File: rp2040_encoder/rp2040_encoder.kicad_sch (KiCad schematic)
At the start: 14 parts, among them J1 Conn_01x05, U1 MT6701, U2 love

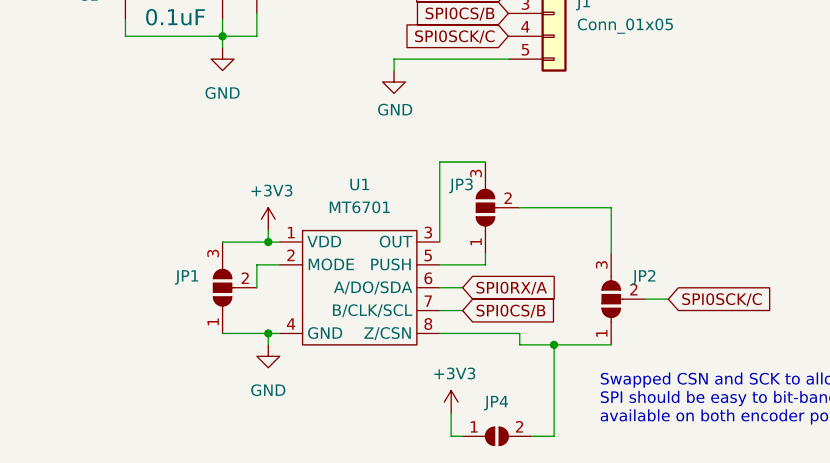
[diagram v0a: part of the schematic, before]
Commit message: updated design with dual CPUs
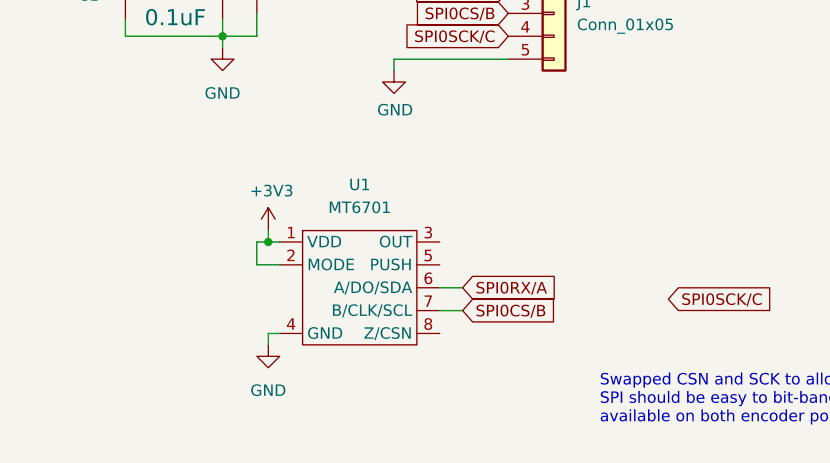
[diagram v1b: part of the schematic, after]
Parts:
- removed JP1, JP2, JP3: SolderJumper_3_Open, Jumper:SolderJumper-3_P1.3mm_Open_RoundedPad1.0x1.5mm_NumberLabels, symbol Jumper:SolderJumper_3_Open
- removed JP4: SolderJumper_2_Open, Jumper:SolderJumper-2_P1.3mm_Open_RoundedPad1.0x1.5mm, symbol Jumper:SolderJumper_2_Open
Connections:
- net +3V3: now also U1.2 (MODE)
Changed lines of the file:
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@@
 (kicad_sch (version 20211123) (generator eeschema)
   (paper "A4")
-  (junction (at 153.67 121.92) (diameter 0) (color 0 0 0 0)
-  )
-  (junction (at 121.92 120.65) (diameter 0) (color 0 0 0 0)
+  (junction (at 121.92 110.49) (diameter 0) (color 0 0 0 0)
   )
   (junction (at 116.84 76.2) (diameter 0) (color 0 0 0 0)
   )
-  (junction (at 121.92 110.49) (diameter 0) (color 0 0 0 0)
-  )
   (junction (at 116.84 87.63) (diameter 0) (color 0 0 0 0)
   )
@@
     (stroke (width 0) (type default) (color 0 0 0 0))
   )
-  (wire (pts (xy 140.97 110.49) (xy 140.97 101.6))
-    (stroke (width 0) (type default) (color 0 0 0 0))
-  )
   (wire (pts (xy 123.19 110.49) (xy 121.92 110.49))
     (stroke (width 0) (type default) (color 0 0 0 0))
   )
-  (wire (pts (xy 160.02 106.68) (xy 160.02 111.76))
-    (stroke (width 0) (type default) (color 0 0 0 0))
-  )
   (wire (pts (xy 120.65 87.63) (xy 120.65 85.09))
     (stroke (width 0) (type default) (color 0 0 0 0))
@@
     (stroke (width 0) (type default) (color 0 0 0 0))
   )
-  (wire (pts (xy 149.86 106.68) (xy 160.02 106.68))
-    (stroke (width 0) (type default) (color 0 0 0 0))
-  )
-  (wire (pts (xy 120.65 113.03) (xy 120.65 115.57))
-    (stroke (width 0) (type default) (color 0 0 0 0))
-  )
   (wire (pts (xy 116.84 76.2) (xy 116.84 78.105))
     (stroke (width 0) (type default) (color 0 0 0 0))
   )
-  (wire (pts (xy 140.97 113.03) (xy 146.05 113.03))
-    (stroke (width 0) (type default) (color 0 0 0 0))
-  )
   (wire (pts (xy 116.84 85.725) (xy 116.84 87.63))
     (stroke (width 0) (type default) (color 0 0 0 0))
@@
     (stroke (width 0) (type default) (color 0 0 0 0))
   )
-  (wire (pts (xy 146.05 113.03) (xy 146.05 111.76))
-    (stroke (width 0) (type default) (color 0 0 0 0))
-  )
-  (wire (pts (xy 116.84 120.65) (xy 121.92 120.65))
-    (stroke (width 0) (type default) (color 0 0 0 0))
-  )
   (wire (pts (xy 116.84 75.565) (xy 116.84 76.2))
     (stroke (width 0) (type default) (color 0 0 0 0))
@@
     (stroke (width 0) (type default) (color 0 0 0 0))
   )
-  (wire (pts (xy 153.67 121.92) (xy 160.02 121.92))
-    (stroke (width 0) (type default) (color 0 0 0 0))
-  )
-  (wire (pts (xy 140.97 101.6) (xy 146.05 101.6))
-    (stroke (width 0) (type default) (color 0 0 0 0))
-  )
   (wire (pts (xy 120.65 77.47) (xy 120.65 76.2))
     (stroke (width 0) (type default) (color 0 0 0 0))
@@
     (stroke (width 0) (type default) (color 0 0 0 0))
   )
-  (wire (pts (xy 116.84 110.49) (xy 121.92 110.49))
-    (stroke (width 0) (type default) (color 0 0 0 0))
-  )
-  (wire (pts (xy 149.86 120.65) (xy 149.86 121.92))
-    (stroke (width 0) (type default) (color 0 0 0 0))
-  )
-  (wire (pts (xy 151.13 132.08) (xy 153.67 132.08))
-    (stroke (width 0) (type default) (color 0 0 0 0))
-  )
   (wire (pts (xy 106.045 76.2) (xy 106.045 78.105))
     (stroke (width 0) (type default) (color 0 0 0 0))
@@
     (stroke (width 0) (type default) (color 0 0 0 0))
   )
-  (wire (pts (xy 163.83 116.84) (xy 166.37 116.84))
+  (wire (pts (xy 120.65 110.49) (xy 121.92 110.49))
     (stroke (width 0) (type default) (color 0 0 0 0))
   )
@@
     (stroke (width 0) (type default) (color 0 0 0 0))
   )
-  (wire (pts (xy 140.97 120.65) (xy 149.86 120.65))
-    (stroke (width 0) (type default) (color 0 0 0 0))
-  )
   (wire (pts (xy 106.045 87.63) (xy 116.84 87.63))
     (stroke (width 0) (type default) (color 0 0 0 0))
   )
-  (wire (pts (xy 142.24 132.08) (xy 142.24 129.54))
+  (wire (pts (xy 120.65 113.03) (xy 120.65 110.49))
     (stroke (width 0) (type default) (color 0 0 0 0))
   )
@@
     (stroke (width 0) (type default) (color 0 0 0 0))
   )
-  (wire (pts (xy 143.51 132.08) (xy 142.24 132.08))
-    (stroke (width 0) (type default) (color 0 0 0 0))
-  )
   (wire (pts (xy 106.045 85.725) (xy 106.045 87.63))
     (stroke (width 0) (type default) (color 0 0 0 0))
   )
   (wire (pts (xy 147.32 80.01) (xy 147.32 78.74))
-    (stroke (width 0) (type default) (color 0 0 0 0))
-  )
-  (wire (pts (xy 149.86 121.92) (xy 153.67 121.92))
-    (stroke (width 0) (type default) (color 0 0 0 0))
-  )
-  (wire (pts (xy 153.67 132.08) (xy 153.67 121.92))
     (stroke (width 0) (type default) (color 0 0 0 0))
   )
@@
       (effects (font (size 1.27 1.27)) hide)
     )
-  )
-  (symbol (lib_id "Jumper:SolderJumper_3_Open") (at 160.02 116.84 90) (unit 1)
-    (in_bom no) (on_board yes)
-    (property "Reference" "JP2" (id 0) (at 165.1 114.2999 90)
-      (effects (font (size 1.27 1.27)) (justify left))
-    )
-    (property "Value" "SolderJumper_3_Open" (id 1) (at 157.48 118.1099 90)
-      (effects (font (size 1.27 1.27)) (justify left) hide)
-    )
-    (property "Footprint" "Jumper:SolderJumper-3_P1.3mm_Open_RoundedPad1.0x1.5mm_NumberLabels" (id 2) (at 160.02 116.84 0)
-      (effects (font (size 1.27 1.27)) hide)
-    )
-    (property "Datasheet" "~" (id 3) (at 160.02 116.84 0)
-      (effects (font (size 1.27 1.27)) hide)
-    )
-    (pin "1")
-    (pin "2")
-    (pin "3")
-  )
-  (symbol (lib_id "Jumper:SolderJumper_3_Open") (at 146.05 106.68 90) (unit 1)
-    (in_bom no) (on_board yes)
-    (property "Reference" "JP3" (id 0) (at 144.78 104.1399 90)
-      (effects (font (size 1.27 1.27)) (justify left))
-    )
-    (property "Value" "SolderJumper_3_Open" (id 1) (at 143.51 107.9499 90)
-      (effects (font (size 1.27 1.27)) (justify left) hide)
-    )
-    (property "Footprint" "Jumper:SolderJumper-3_P1.3mm_Open_RoundedPad1.0x1.5mm_NumberLabels" (id 2) (at 146.05 106.68 0)
-      (effects (font (size 1.27 1.27)) hide)
-    )
-    (property "Datasheet" "~" (id 3) (at 146.05 106.68 0)
-      (effects (font (size 1.27 1.27)) hide)
-    )
-    (pin "1")
-    (pin "2")
-    (pin "3")
   )
   (symbol (lib_id "power:GND") (at 116.84 88.9 0) (unit 1)
@@
     (pin "1")
   )
-  (symbol (lib_id "Jumper:SolderJumper_2_Open") (at 147.32 132.08 0) (unit 1)
-    (in_bom no) (on_board yes) (fields_autoplaced)
-    (property "Reference" "JP4" (id 0) (at 147.32 128.27 0))
-    (property "Value" "SolderJumper_2_Open" (id 1) (at 147.32 128.27 0)
-      (effects (font (size 1.27 1.27)) hide)
-    )
-    (property "Footprint" "Jumper:SolderJumper-2_P1.3mm_Open_RoundedPad1.0x1.5mm" (id 2) (at 147.32 132.08 0)
-      (effects (font (size 1.27 1.27)) hide)
-    )
-    (property "Datasheet" "~" (id 3) (at 147.32 132.08 0)
-      (effects (font (size 1.27 1.27)) hide)
-    )
-    (pin "1")
-    (pin "2")
-  )
   (symbol (lib_id "power:GND") (at 135.89 91.44 0) (unit 1)
     (in_bom yes) (on_board yes)
@@
     )
   )
-  (symbol (lib_id "power:+3V3") (at 142.24 129.54 0) (unit 1)
-    (in_bom yes) (on_board yes)
-    (property "Reference" "#PWR0101" (id 0) (at 142.24 133.35 0)
-      (effects (font (size 1.27 1.27)) hide)
-    )
-    (property "Value" "+3V3" (id 1) (at 142.621 125.1458 0))
-    (property "Footprint" "" (id 2) (at 142.24 129.54 0)
-      (effects (font (size 1.27 1.27)) hide)
-    )
-    (property "Datasheet" "" (id 3) (at 142.24 129.54 0)
-      (effects (font (size 1.27 1.27)) hide)
-    )
-    (pin "1")
-  )
   (symbol (lib_id "encoder_parts:love") (at 67.31 105.41 0) (unit 1)
     (in_bom yes) (on_board yes) (fields_autoplaced)
@@
     )
     (pin "1")
-  )
-  (symbol (lib_id "Jumper:SolderJumper_3_Open") (at 116.84 115.57 90) (unit 1)
-    (in_bom no) (on_board yes) (fields_autoplaced)
-    (property "Reference" "JP1" (id 0) (at 114.3 114.2999 90)
-      (effects (font (size 1.27 1.27)) (justify left))
-    )
-    (property "Value" "SolderJumper_3_Open" (id 1) (at 114.3 116.8399 90)
-      (effects (font (size 1.27 1.27)) (justify left) hide)
-    )
-    (property "Footprint" "Jumper:SolderJumper-3_P1.3mm_Open_RoundedPad1.0x1.5mm_NumberLabels" (id 2) (at 116.84 115.57 0)
-      (effects (font (size 1.27 1.27)) hide)
-    )
-    (property "Datasheet" "~" (id 3) (at 116.84 115.57 0)
-      (effects (font (size 1.27 1.27)) hide)
-    )
-    (pin "1")
-    (pin "2")
-    (pin "3")
   )
   (symbol (lib_id "MotorController:SPARKFUN-CAPACITORS_CAP") (at 116.84 83.185 0) (unit 1)
@@
       (reference "#PWR06") (unit 1) (value "+3V3") (footprint "")
     )
-    (path "/9e25af1d-946b-4791-bad3-de4b3bb70174"
-      (reference "#PWR0101") (unit 1) (value "+3V3") (footprint "")
-    )
     (path "/d4beee8a-fda6-4644-a94b-f51a39e75e2f"
       (reference "C1") (unit 1) (value "1u") (footprint "Capacitor_SMD:C_0603_1608Metric")
@@
       (reference "J1") (unit 1) (value "Conn_01x05") (footprint "parts:Molex_KK-254_1x05_P2.54mm_Horizontal")
     )
-    (path "/fe21cad9-d1c8-4802-ac2f-c303319ad339"
-      (reference "JP1") (unit 1) (value "SolderJumper_3_Open") (footprint "Jumper:SolderJumper-3_P1.3mm_Open_RoundedPad1.0x1.5mm_NumberLabels")
-    )
-    (path "/082b05b3-53da-4ea9-a411-decf9bf41570"
-      (reference "JP2") (unit 1) (value "SolderJumper_3_Open") (footprint "Jumper:SolderJumper-3_P1.3mm_Open_RoundedPad1.0x1.5mm_NumberLabels")
-    )
-    (path "/26bf0a5f-7f16-4e2d-a109-4f3c06734dcd"
-      (reference "JP3") (unit 1) (value "SolderJumper_3_Open") (footprint "Jumper:SolderJumper-3_P1.3mm_Open_RoundedPad1.0x1.5mm_NumberLabels")
-    )
-    (path "/617c9a7e-46cc-41ce-960c-49043682abc3"
-      (reference "JP4") (unit 1) (value "SolderJumper_2_Open") (footprint "Jumper:SolderJumper-2_P1.3mm_Open_RoundedPad1.0x1.5mm")
-    )
     (path "/555c8940-ebb2-464f-8b26-adbbd6ba117c"

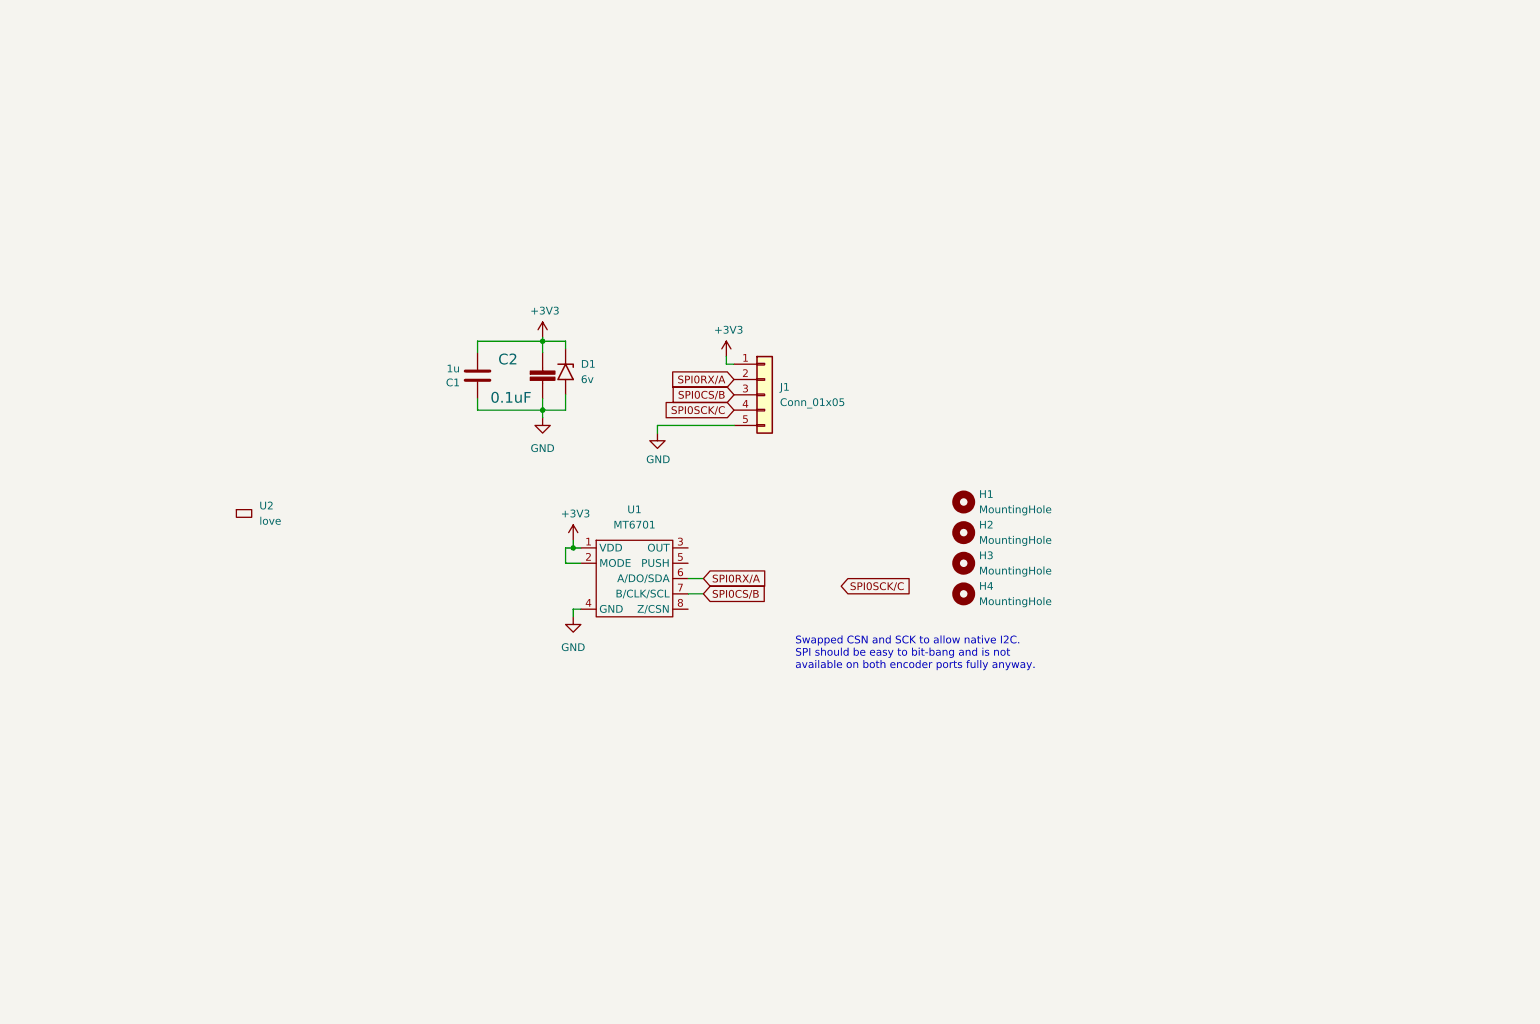
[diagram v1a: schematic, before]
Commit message: Add encoder, update readme
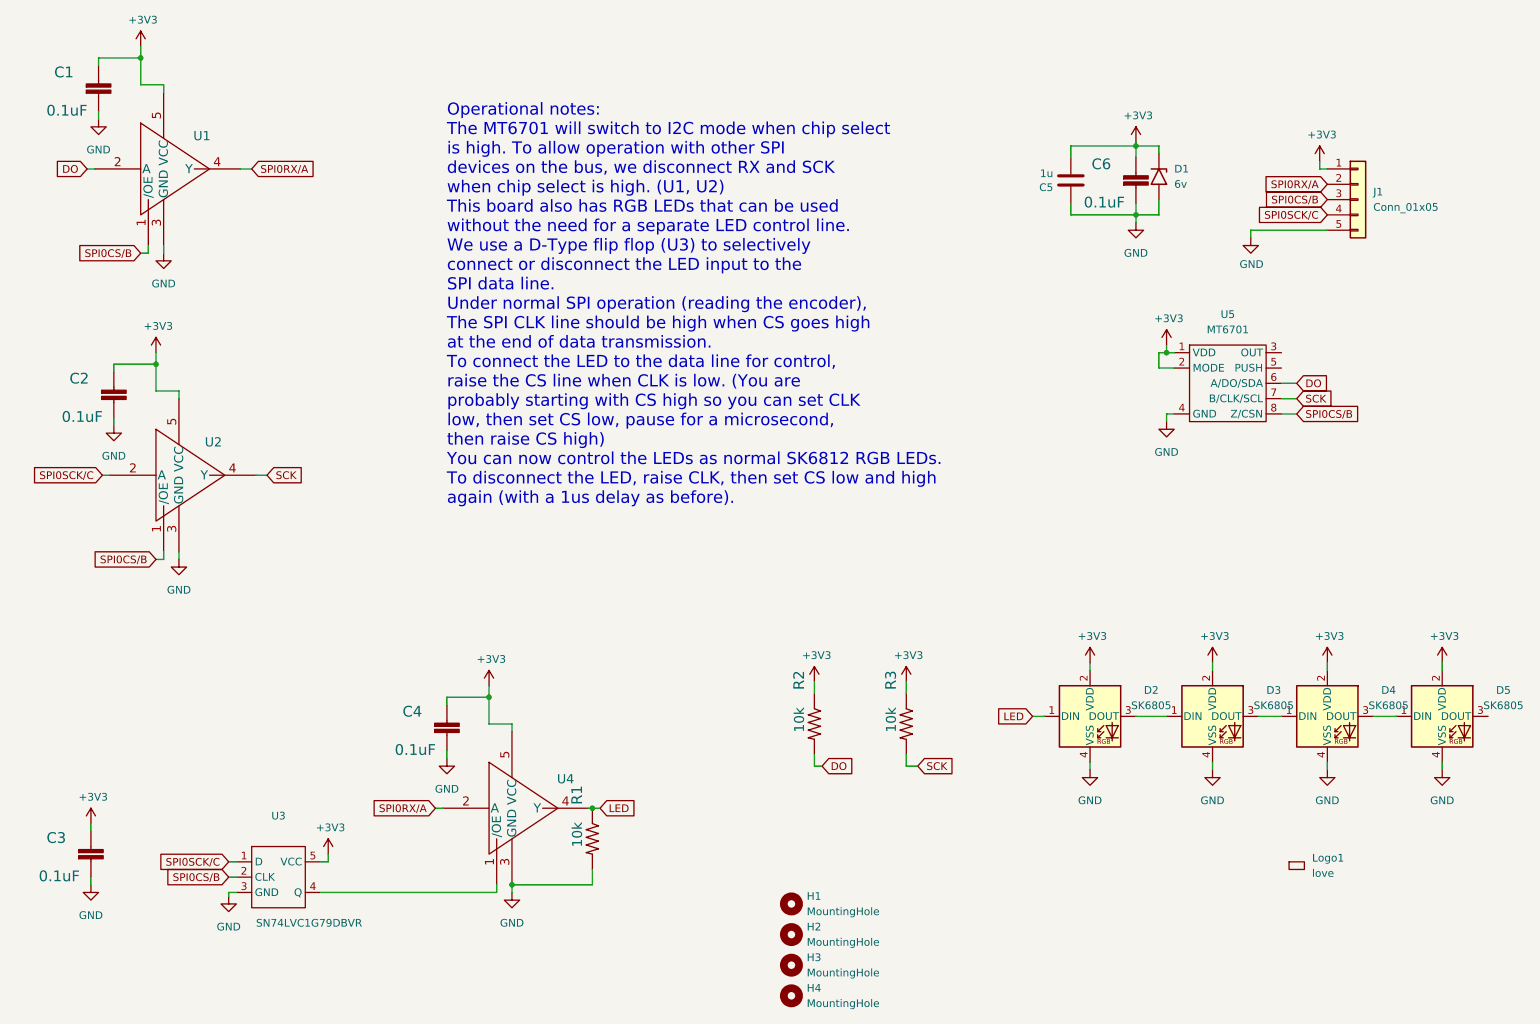
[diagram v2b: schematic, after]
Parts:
- added C1, C2, C3, C4: 0.1uF, Capacitor_SMD:C_0603_1608Metric, symbol MotorController:SPARKFUN-CAPACITORS_CAP
- added D2, D3, D4, D5: SK6805, LED_SMD:LED_SK6812_EC15_1.5x1.5mm, symbol encoder_parts:SK6805-EC15
- added R1, R2, R3: 10k, Resistor_SMD:R_0603_1608Metric, symbol MotorController:TAYLOR_RESISTOR
- added U1, U2, U4: SN74LVC1G07QDCKTQ1, Package_TO_SOT_SMD:SOT-353_SC-70-5, symbol acorn-motherboard:SN74LVC1G07QDCKTQ1
- added U3: SN74LVC1G79DBVR, Package_TO_SOT_SMD:SOT-353_SC-70-5, symbol encoder_parts:SN74LVC1G80DCKR
- Logo1: renamed from U2; now left out of the parts list
- renumbered C1 to C5, C2 to C6, U1 to U5
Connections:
- net +3V3: now also C1.1, C2.1, C3.1, C4.1, D2.2 (VDD), D3.2 (VDD), D4.2 (VDD), D5.2 (VDD), R2.1, R3.1, U1.5 (VCC), U2.5 (VCC), U3.5 (VCC), U4.5 (VCC)
- net GND: now also C1.2, C2.2, C3.2, C4.2, D2.4 (VSS), D3.4 (VSS), D4.4 (VSS), D5.4 (VSS), R1.2, U1.3 (GND), U2.3 (GND), U3.3 (GND), U4.3 (GND)
- net SPI0CS/B: now also U5.8 (Z/CSN), U1.1 (/OE), U2.1 (/OE), U3.2 (CLK); no longer U5.7 (B/CLK/SCL)
- net SPI0RX/A: now also U1.4 (Y), U4.2 (A); no longer U5.6 (A/DO/SDA)
- net SPI0SCK/C: now also U2.2 (A), U3.1 (D)
- new net: U3.4 (Q), U4.1 (/OE)
- new net: D2.3 (DOUT), D3.1 (DIN)
- new net: D4.3 (DOUT), D5.1 (DIN)
- new net: D3.3 (DOUT), D4.1 (DIN)
- new net DO: R2.2, U1.2 (A), U5.6 (A/DO/SDA)
- new net LED: D2.1 (DIN), R1.1, U4.4 (Y)
- new net SCK: R3.2, U2.4 (Y), U5.7 (B/CLK/SCL)
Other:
- note added: "Operational notes: The MT6701 will switch to I2C mode when chip select is high. To allow operation with other SPI devices on the bus, we disconnect RX and SCK when chip select is high. (U1, U2) This board also has RGB LEDs that can be used without the need for a separate LED control line. We use a D-Type flip flop (U3) to selectively connect or disconnect the LED input to the SPI data line. Under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"
- note removed: "Swapped CSN and SCK to allow native I2C. SPI should be easy to bit-bang and is not available on both encoder ports fully anyway."
- moved on the sheet: C5, C6, D1, H1, H2, H3, H4, J1, Logo1, U5

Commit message: Update boards for latest build, pending design review.
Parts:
- removed C1, C2, C3, C4: 0.1uF, Capacitor_SMD:C_0603_1608Metric, symbol MotorController:SPARKFUN-CAPACITORS_CAP
- removed D2, D3, D4, D5: SK6805, LED_SMD:LED_SK6812_EC15_1.5x1.5mm, symbol encoder_parts:SK6805-EC15
- removed J1: Conn_01x05, parts:Molex_KK-254_1x05_P2.54mm_Horizontal, symbol Connector_Generic:Conn_01x05
- removed R1, R2, R3: 10k, Resistor_SMD:R_0603_1608Metric, symbol MotorController:TAYLOR_RESISTOR
- removed U1, U2, U4: SN74LVC1G07QDCKTQ1, Package_TO_SOT_SMD:SOT-353_SC-70-5, symbol acorn-motherboard:SN74LVC1G07QDCKTQ1
- removed U3: SN74LVC1G79DBVR, Package_TO_SOT_SMD:SOT-353_SC-70-5, symbol encoder_parts:SN74LVC1G80DCKR
- added J1: Conn_01x02, Connector_PinHeader_2.54mm:PinHeader_1x02_P2.54mm_Vertical, symbol Connector_Generic:Conn_01x02
- added J2: Conn_01x06, parts:Molex_KK-254_1x06_P2.54mm_Horizontal, symbol Connector_Generic:Conn_01x06
- added R1, R2, R3: 100R, Resistor_SMD:R_0603_1608Metric, symbol Device:R
- added TH1: Thermistor 10k, Resistor_SMD:R_0603_1608Metric, symbol Device:Thermistor_NTC
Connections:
- net DO is gone; now on net SPI0RX/A: U5.6 (A/DO/SDA)
- net SCK is gone; now on net SPI0SCK/C: U5.7 (B/CLK/SCL)
- net +3V3: now also J1.1 (Pin_1), J2.1 (Pin_1), TH1.1
- net GND: now also J2.5 (Pin_5)
- net SPI0CS/B: now also R1.2
- net SPI0RX/A: now also R3.2
- net SPI0SCK/C: now also R2.2
- new net: J2.4 (Pin_4), R2.1
- new net: J2.2 (Pin_2), R3.1
- new net: J2.3 (Pin_3), R1.1
- new net TH1_SENSE: J1.2 (Pin_2), J2.6 (Pin_6), TH1.2
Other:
- note added: "FOR EXTERNAL THERMISTOR"
- note removed: "Operational notes: The MT6701 will switch to I2C mode when chip select is high. To allow operation with other SPI devices on the bus, we disconnect RX and SCK when chip select is high. (U1, U2) This board also has RGB LEDs that can be used without the need for a separate LED control line. We use a D-Type flip flop (U3) to selectively connect or disconnect the LED input to the SPI data line. Under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"
- moved on the sheet: C5, C6, D1, U5

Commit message: Updated files for boards ordered July 2024
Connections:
- no-connect marks 0 -> 3
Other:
- moved on the sheet: C5, C6, D1, H1, H2, H3, H4, J1, J2, Logo1, R1, R2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
